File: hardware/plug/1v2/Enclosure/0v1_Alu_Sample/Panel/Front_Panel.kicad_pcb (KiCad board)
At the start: 2 copper layers, 65.8 x 42.7 mm, 11 parts

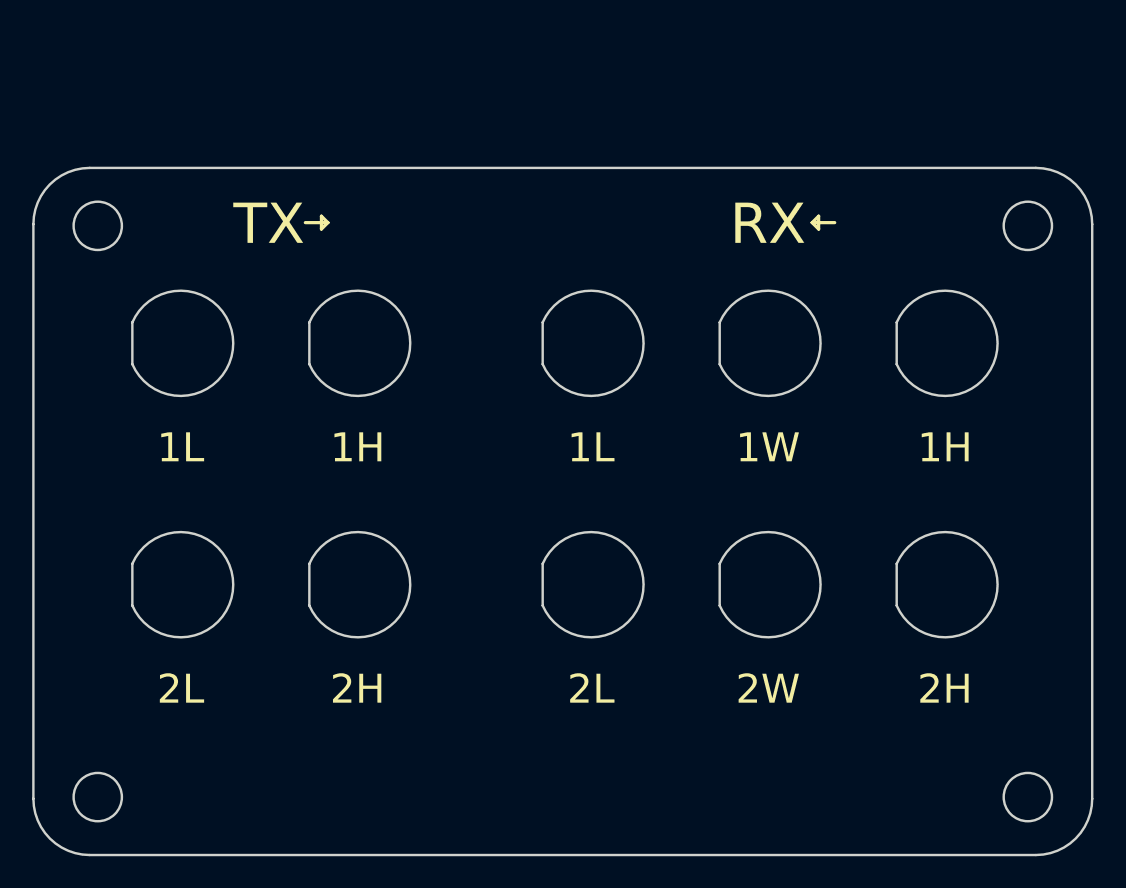
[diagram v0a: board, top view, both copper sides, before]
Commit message: 0v2 in dev
- mockup LimeSDR made
- partially completed 0v1 enclosure (front panel)
- ordered new wider enclosures
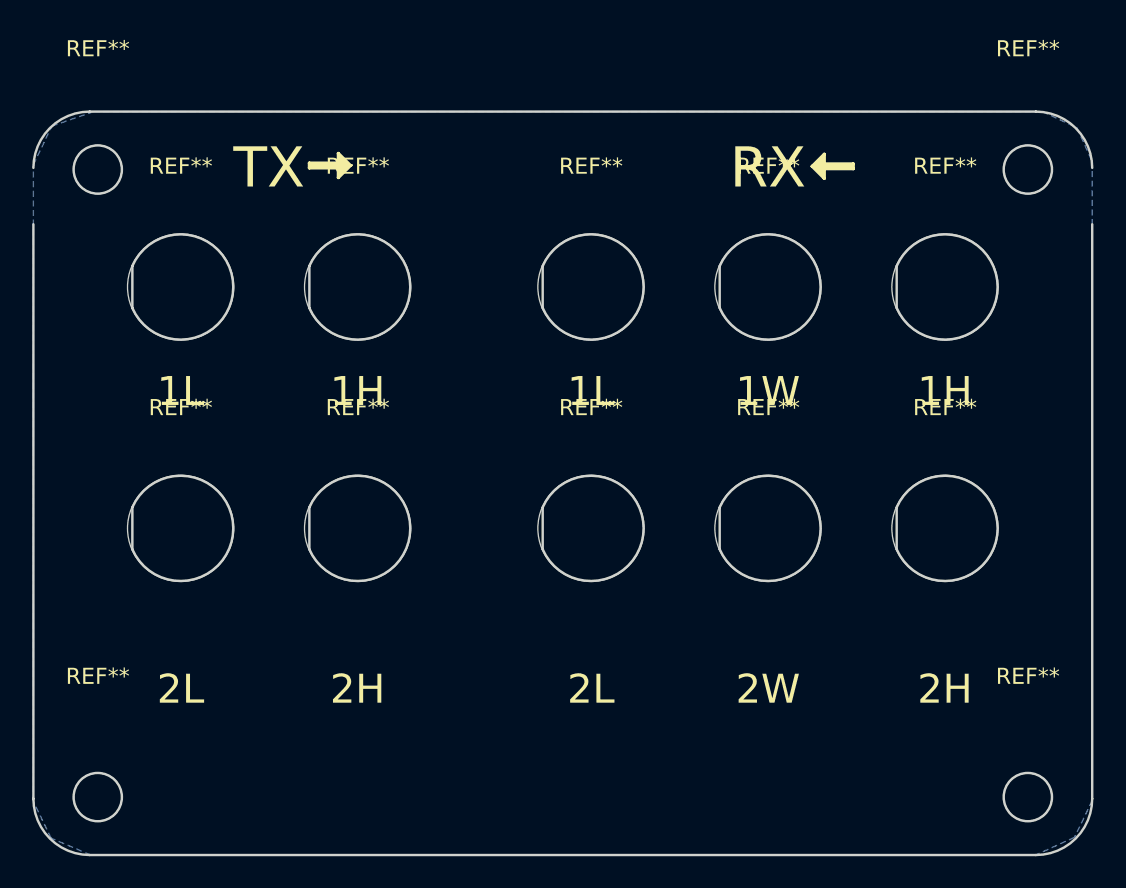
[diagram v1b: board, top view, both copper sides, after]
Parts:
- added REF**: MountingHole_6.5mm, Mounting_Holes:MountingHole_6.5mm, F.Cu at (162.8, 38.9)
- added REF**: MountingHole_6.5mm, Mounting_Holes:MountingHole_6.5mm, F.Cu at (135.6, 46.2)
- added REF**: MountingHole_6.5mm, Mounting_Holes:MountingHole_6.5mm, F.Cu at (121.1, 61.2)
- added REF**: MountingHole_6.5mm, Mounting_Holes:MountingHole_6.5mm, F.Cu at (110.1, 61.2)
- added REF**: MountingHole_6.5mm, Mounting_Holes:MountingHole_6.5mm, F.Cu at (121.1, 46.2)
- added REF**: MountingHole_6.5mm, Mounting_Holes:MountingHole_6.5mm, F.Cu at (105.0, 38.9)
- added REF**: MountingHole_6.5mm, Mounting_Holes:MountingHole_6.5mm, F.Cu at (110.1, 46.2)
- added REF**: MountingHole_6.5mm, Mounting_Holes:MountingHole_6.5mm, F.Cu at (105.0, 77.9)
- added REF**: MountingHole_6.5mm, Mounting_Holes:MountingHole_6.5mm, F.Cu at (162.8, 77.9)
- added REF**: MountingHole_6.5mm, Mounting_Holes:MountingHole_6.5mm, F.Cu at (135.6, 61.2)
- added REF**: MountingHole_6.5mm, Mounting_Holes:MountingHole_6.5mm, F.Cu at (146.6, 61.2)
- added REF**: MountingHole_6.5mm, Mounting_Holes:MountingHole_6.5mm, F.Cu at (157.6, 61.2)
- added REF**: MountingHole_6.5mm, Mounting_Holes:MountingHole_6.5mm, F.Cu at (157.6, 46.2)
- added REF**: MountingHole_6.5mm, Mounting_Holes:MountingHole_6.5mm, F.Cu at (146.6, 46.2)
- moved REF** 3.50 mm to (157.6, 46.2)
- moved REF** 3.50 mm to (135.6, 61.2)
- moved REF** 3.50 mm to (146.6, 61.2)
- moved REF** 3.50 mm to (157.6, 61.2)
- moved REF** 3.50 mm to (135.6, 46.2)
- moved REF** 3.50 mm to (146.6, 46.2)
- moved REF** 3.50 mm to (121.1, 61.2)
- moved REF** 3.50 mm to (110.1, 61.2)
- moved REF** 3.50 mm to (121.1, 46.2)
- moved REF** 3.50 mm to (110.1, 46.2)
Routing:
- added copper zone on B.Cu, net (none)
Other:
- board size 65.8 x 42.7 mm -> 65.8 x 46.2 mm
